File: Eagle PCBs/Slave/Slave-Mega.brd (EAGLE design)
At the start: 87.3 x 40.6 mm, 15 parts

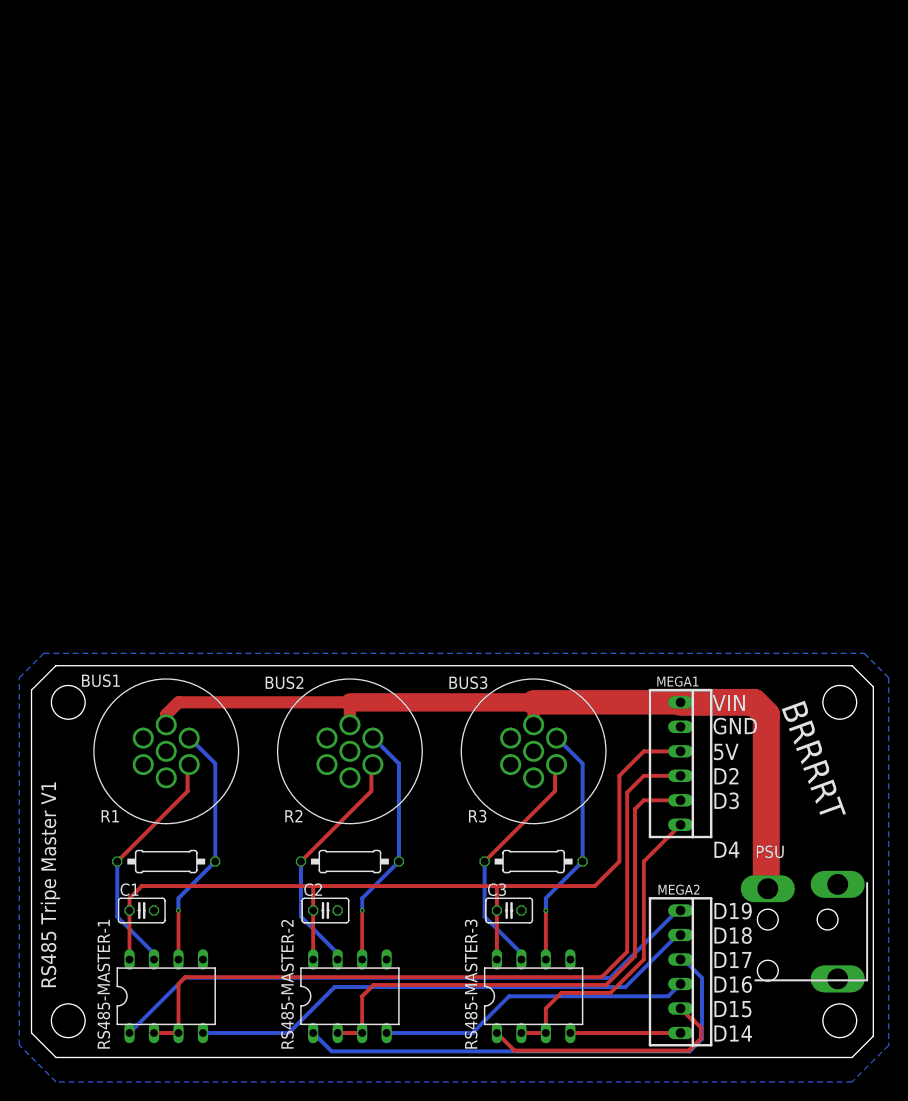
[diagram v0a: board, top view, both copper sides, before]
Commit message: New mega slave PCB Increased clearances on master PCB
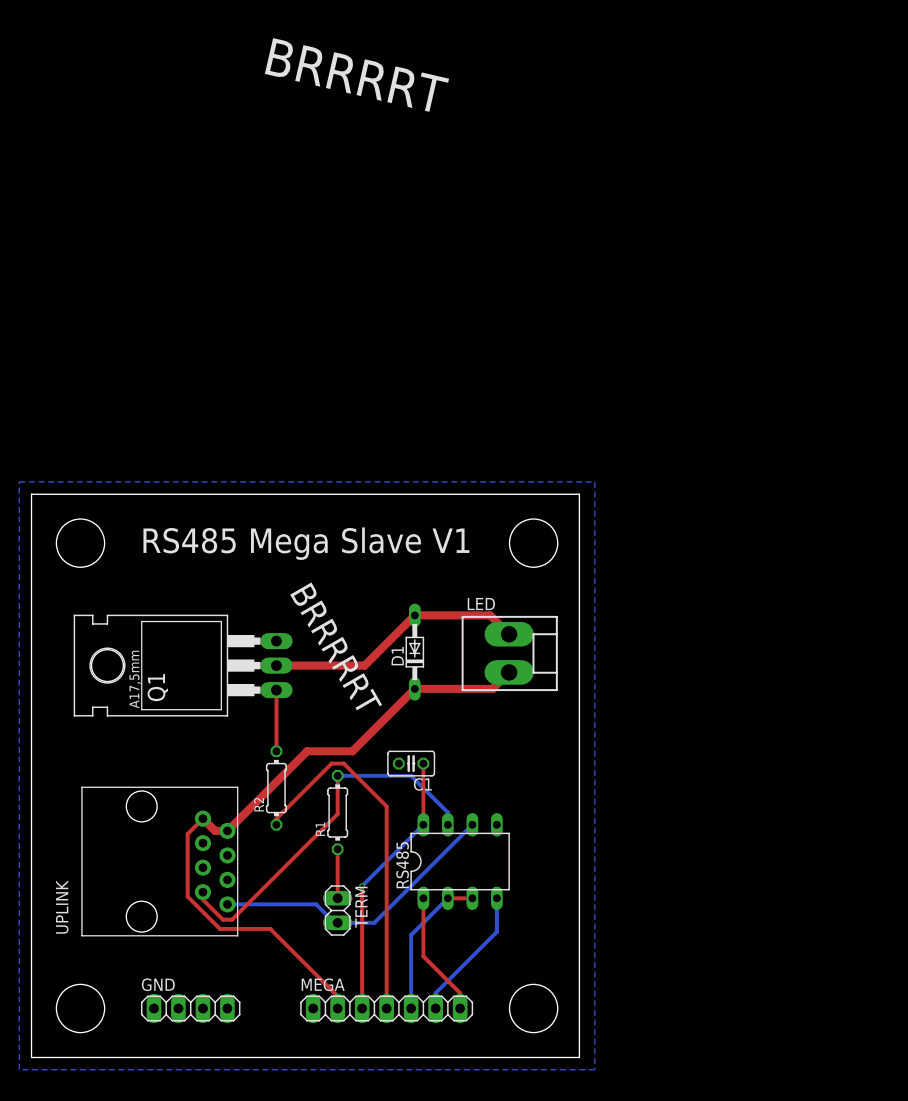
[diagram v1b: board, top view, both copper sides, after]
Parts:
- removed BUS1, BUS2, BUS3: GX12-7P, A10 Library:GX12-7P
- removed C2, C3: 0.1uF, rcl:C025-025X050
- removed MEGA1, MEGA2: 6P, con-molex:22-23-2061
- removed PSU: DC-044A, A10 Library:DC-044A
- removed R3: 120Ω, rcl:0207/10
- removed RS485-MASTER-1, RS485-MASTER-2, RS485-MASTER-3: MAX487CPA, A10 Library:DIL08
- added D1: BAT81, diode:DO34-7
- added GND: (no value), pinhead:1X04
- added LED: (no value), con-molex:KK-156-2
- added MEGA: (no value), pinhead:1X07
- added Q1: TIP120, transistor-power:TO220AH
- added RS485: MAX487CPA, A10 Library:DIL08
- added TERM: (no value), pinhead:1X02
- added UPLINK: RJ45-8P8C, A10 Library:RJ45-8P8C
- R1: device rcl:0207/10 -> rcl:0204/7
- R2: value 120Ω -> 1K; device rcl:0207/10 -> rcl:0204/7
- moved C1 31.8 mm to (39.4, 30.5), turned to 180 degrees
- moved R1 18.5 mm to (31.8, 25.4), turned to 90 degrees
- moved R2 10.8 mm to (25.4, 27.9), turned to 90 degrees
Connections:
- removed net MEGA_D14: MEGA2.6, RS485-MASTER-3.4
- removed net MEGA_D15: MEGA2.5, RS485-MASTER-3.1
- removed net MEGA_D16: MEGA2.4, RS485-MASTER-2.4
- removed net MEGA_D17: MEGA2.3, RS485-MASTER-2.1
- removed net MEGA_D18: MEGA2.2, RS485-MASTER-1.4
- removed net MEGA_D19: MEGA2.1, RS485-MASTER-1.1
- removed net MEGA_D4: MEGA1.6, RS485-MASTER-3.2, RS485-MASTER-3.3
- removed net RS485_1_A: BUS1.2, R1.2, RS485-MASTER-1.6
- removed net RS485_1_B: BUS1.3, R1.1, RS485-MASTER-1.7
- removed net RS485_2_A: BUS2.2, R2.2, RS485-MASTER-2.6
- removed net RS485_2_B: BUS2.3, R2.1, RS485-MASTER-2.7
- removed net RS485_3_A: BUS3.2, R3.2, RS485-MASTER-3.6
- removed net RS485_3_B: BUS3.3, R3.1, RS485-MASTER-3.7
- removed net VCC: BUS1.1, BUS2.1, BUS3.1, MEGA1.1, PSU.1
- new net LED_GND: D1.A, LED.1, Q1.C
- new net LED_PWM: Q1.B, R2.2
- new net MEGA_RX: MEGA.7, RS485.1
- new net MEGA_TX: MEGA.6, RS485.4
- new net RS485_A: RS485.6, TERM.2, UPLINK.8
- new net RS485_B: R1.2, RS485.7, UPLINK.7
- new net TERM: R1.1, TERM.1
- new net VDD: D1.C, LED.2, MEGA.2, UPLINK.1, UPLINK.2
- net 5VCC: now also MEGA.3, RS485.8; no longer C2.1, C3.1, MEGA1.3, RS485-MASTER-1.8, RS485-MASTER-2.8, RS485-MASTER-3.8
- net GND: now also GND.1, GND.2, GND.3, GND.4, MEGA.1, Q1.E, RS485.5, UPLINK.3, UPLINK.4; no longer BUS1.6, BUS2.6, BUS3.6, C2.2, C3.2, MEGA1.2, PSU.GND, PSU.GND-2, RS485-MASTER-1.5, RS485-MASTER-2.5, RS485-MASTER-3.5
- net MEGA_D2: now also MEGA.5, RS485.2, RS485.3; no longer MEGA1.4, RS485-MASTER-1.2, RS485-MASTER-1.3
- net MEGA_D3: now also MEGA.4, R2.1; no longer MEGA1.5, RS485-MASTER-2.2, RS485-MASTER-2.3
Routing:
- net VCC: track 87.1 -> 0.00 mm
- net VDD: track 0.00 -> 68.9 mm
- net MEGA_D2: track 78.3 -> 15.5 mm
- net MEGA_D19: track 62.4 -> 0.00 mm
- net 5VCC: track 90.3 -> 28.0 mm, vias 0 -> 1
- net MEGA_D18: track 53.7 -> 0.00 mm
- net MEGA_D17: track 51.0 -> 0.00 mm
- net RS485_B: track 0.00 -> 38.4 mm
- net MEGA_D4: track 32.9 -> 0.00 mm
- net MEGA_D16: track 32.6 -> 0.00 mm
- net RS485_A: track 0.00 -> 30.4 mm
- net LED_GND: track 0.00 -> 27.1 mm
- net MEGA_D15: track 26.5 -> 0.00 mm
- net RS485_2_A: track 25.7 -> 0.00 mm, vias 1 -> 0
- net RS485_1_A: track 25.7 -> 0.00 mm, vias 1 -> 0
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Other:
- board size 87.3 x 40.6 mm -> 56.8 x 58.4 mm
- board text added: "BRRRRRT"
- board text added: "RS485 Mega Slave V1"
- board text removed: "5V"
- board text removed: "D14"
- board text removed: "D15"
- board text removed: "D16"
- board text removed: "D17"
- board text removed: "D18"
- board text removed: "D19"
- board text removed: "D2"
- board text removed: "D3"
- board text removed: "D4"
- board text removed: "GND"
- board text removed: "RS485 Tripe Master V1"
- board text removed: "VIN"
